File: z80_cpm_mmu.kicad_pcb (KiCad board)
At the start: 2 copper layers, 102.9 x 22.9 mm, 17 parts, among them P1 BUS, P2 ROM, P3 OUT, P4 RAM, P5 AUX, P6 EXT, U1 74HCT04, U3 74LS32, U4 74HCT00

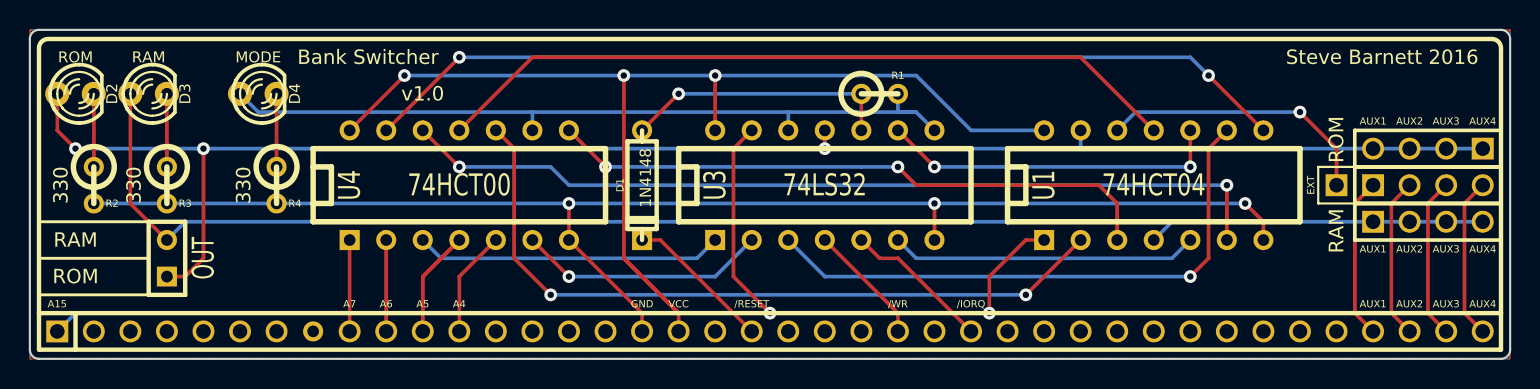
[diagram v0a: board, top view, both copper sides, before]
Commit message: Fix IC references to be contiguous
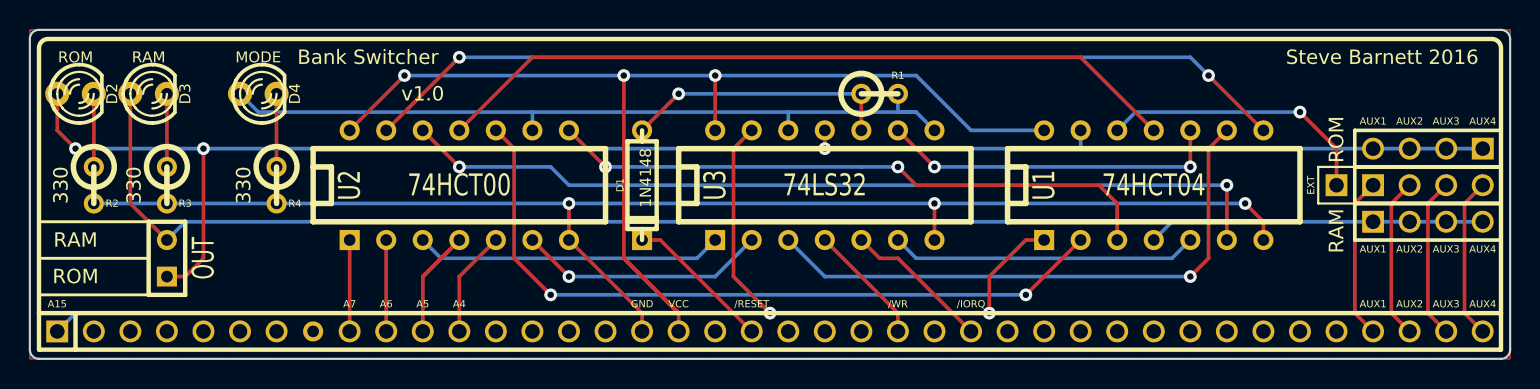
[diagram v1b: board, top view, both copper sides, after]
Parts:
- removed U4: 74HCT00, DIP-14__300
- added U2: 74HCT00, DIP-14__300, F.Cu at (143.5, 94.0)

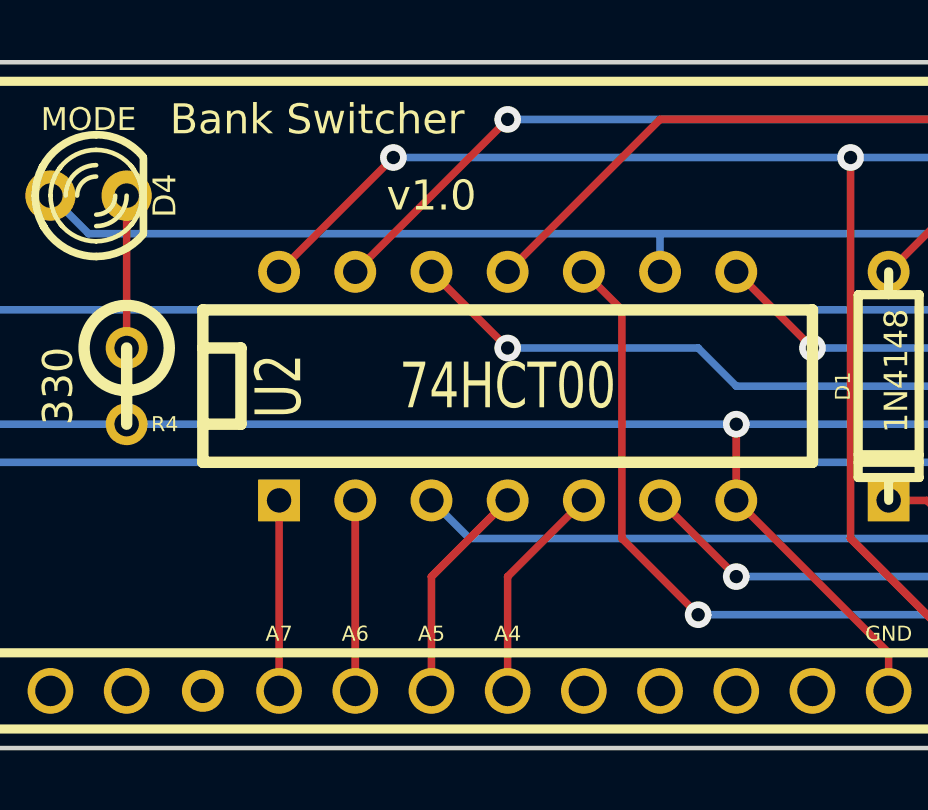
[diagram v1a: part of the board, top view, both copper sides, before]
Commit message: Begin work on v1.1 - fix size of bus pad 8
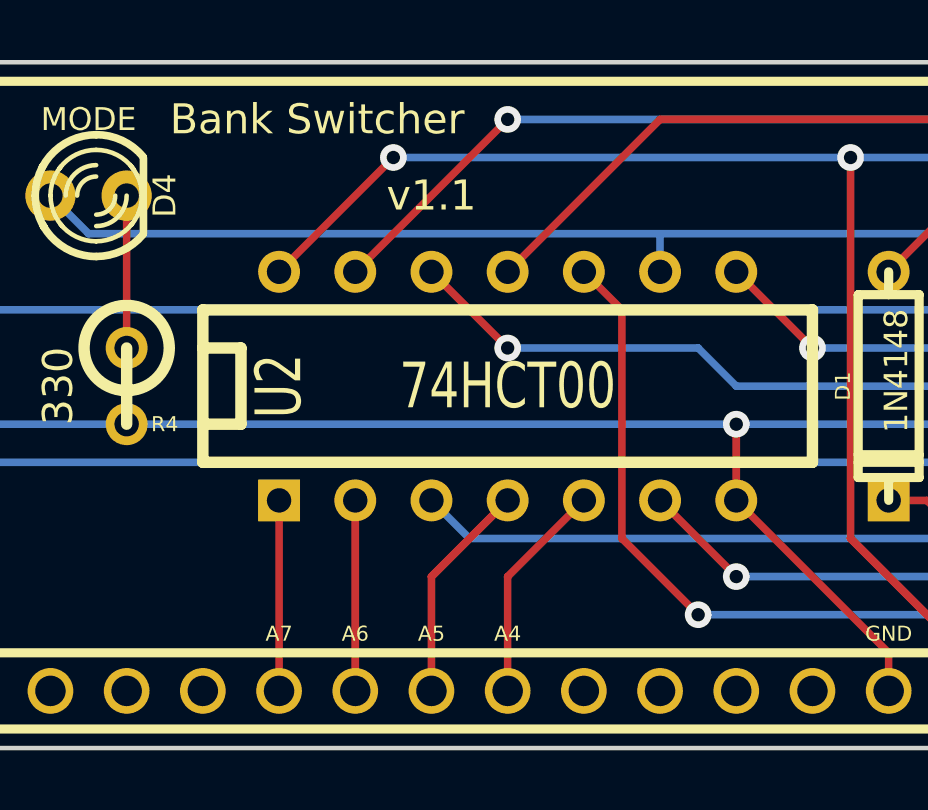
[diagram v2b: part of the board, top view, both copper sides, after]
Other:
- board text added: "v1.1"
- board text removed: "v1.0"
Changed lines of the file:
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@@
     (links 55)
     (no_connects 0)
-    (area 113.589999 83.109999 216.610001 106.120001)
+    (area 110.617 83.109999 220.5736 106.214333)
     (thickness 1.6)
     (drawings 54)
@@
       (layers *.Cu *.Mask F.SilkS)
     )
-    (pad 8 thru_hole circle (at -3.81 0) (size 1.397 1.397) (drill 0.812799)
+    (pad 8 thru_hole circle (at -3.81 0) (size 1.524 1.524) (drill 1.016)
       (layers *.Cu *.Mask F.SilkS)
     )
@@
     (fp_line (start -8.89 1.27) (end -10.16 1.27) (layer F.SilkS) (width 0.381))
     (fp_line (start 10.16 -2.54) (end 10.16 2.54) (layer F.SilkS) (width 0.381))
-    (pad 1 thru_hole rect (at -7.62 3.81) (size 1.397 1.397) (drill 0.8128)
+    (pad 1 thru_hole rect (at -7.62 3.81) (size 1.397 1.397) (drill 0.812799)
       (layers *.Cu *.Mask F.SilkS)
       (net 7 /A7)
     )
-    (pad 2 thru_hole circle (at -5.08 3.81) (size 1.397 1.397) (drill 0.8128)
+    (pad 2 thru_hole circle (at -5.08 3.81) (size 1.397 1.397) (drill 0.812799)
       (layers *.Cu *.Mask F.SilkS)
       (net 6 /A6)
     )
-    (pad 3 thru_hole circle (at -2.54 3.81) (size 1.397 1.397) (drill 0.8128)
+    (pad 3 thru_hole circle (at -2.54 3.81) (size 1.397 1.397) (drill 0.812799)
       (layers *.Cu *.Mask F.SilkS)
       (net 29 N-0000056)
     )
-    (pad 4 thru_hole circle (at 0 3.81) (size 1.397 1.397) (drill 0.8128)
+    (pad 4 thru_hole circle (at 0 3.81) (size 1.397 1.397) (drill 0.812799)
       (layers *.Cu *.Mask F.SilkS)
       (net 5 /A5)
     )
-    (pad 5 thru_hole circle (at 2.54 3.81) (size 1.397 1.397) (drill 0.8128)
+    (pad 5 thru_hole circle (at 2.54 3.81) (size 1.397 1.397) (drill 0.812799)
       (layers *.Cu *.Mask F.SilkS)
       (net 4 /A4)
     )
-    (pad 6 thru_hole circle (at 5.08 3.81) (size 1.397 1.397) (drill 0.8128)
+    (pad 6 thru_hole circle (at 5.08 3.81) (size 1.397 1.397) (drill 0.812799)
       (layers *.Cu *.Mask F.SilkS)
       (net 31 N-0000058)
     )
-    (pad 7 thru_hole circle (at 7.62 3.81) (size 1.397 1.397) (drill 0.8128)
+    (pad 7 thru_hole circle (at 7.62 3.81) (size 1.397 1.397) (drill 0.812799)
       (layers *.Cu *.Mask F.SilkS)
       (net 16 GND)
     )
-    (pad 8 thru_hole circle (at 7.62 -3.81) (size 1.397 1.397) (drill 0.8128)
+    (pad 8 thru_hole circle (at 7.62 -3.81) (size 1.397 1.397) (drill 0.812799)
       (layers *.Cu *.Mask F.SilkS)
       (net 26 N-0000049)
     )
-    (pad 9 thru_hole circle (at 5.08 -3.81) (size 1.397 1.397) (drill 0.8128)
+    (pad 9 thru_hole circle (at 5.08 -3.81) (size 1.397 1.397) (drill 0.812799)
       (layers *.Cu *.Mask F.SilkS)
       (net 15 /mode)
     )
-    (pad 10 thru_hole circle (at 2.54 -3.81) (size 1.397 1.397) (drill 0.8128)
+    (pad 10 thru_hole circle (at 2.54 -3.81) (size 1.397 1.397) (drill 0.812799)
       (layers *.Cu *.Mask F.SilkS)
       (net 27 N-0000054)
     )
-    (pad 11 thru_hole circle (at 0 -3.81) (size 1.397 1.397) (drill 0.8128)
+    (pad 11 thru_hole circle (at 0 -3.81) (size 1.397 1.397) (drill 0.812799)
       (layers *.Cu *.Mask F.SilkS)
       (net 18 N-0000025)
     )
-    (pad 12 thru_hole circle (at -2.54 -3.81) (size 1.397 1.397) (drill 0.8128)
+    (pad 12 thru_hole circle (at -2.54 -3.81) (size 1.397 1.397) (drill 0.812799)
       (layers *.Cu *.Mask F.SilkS)
       (net 20 N-0000034)
     )
-    (pad 13 thru_hole circle (at -5.08 -3.81) (size 1.397 1.397) (drill 0.8128)
+    (pad 13 thru_hole circle (at -5.08 -3.81) (size 1.397 1.397) (drill 0.812799)
       (layers *.Cu *.Mask F.SilkS)
       (net 19 N-0000029)
     )
-    (pad 14 thru_hole circle (at -7.62 -3.81) (size 1.397 1.397) (drill 0.8128)
+    (pad 14 thru_hole circle (at -7.62 -3.81) (size 1.397 1.397) (drill 0.812799)
       (layers *.Cu *.Mask F.SilkS)
       (net 32 VCC)
@@
     (effects (font (size 1 1) (thickness 0.25)) (justify mirror))
   )
-  (gr_text v1.0 (at 205.74 87.63) (layer B.SilkS)
+  (gr_text v1.1 (at 205.74 87.63) (layer B.SilkS)
     (effects (font (size 1 1) (thickness 0.25)) (justify mirror))
   )
@@
     (effects (font (size 0.5 0.5) (thickness 0.125)))
   )
-  (gr_text v1.0 (at 140.97 87.63) (layer F.SilkS)
+  (gr_text v1.1 (at 140.97 87.63) (layer F.SilkS)
     (effects (font (size 1 1) (thickness 0.25)))
   )
